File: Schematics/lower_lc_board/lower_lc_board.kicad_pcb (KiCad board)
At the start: 4 copper layers, 69.5 x 60 mm, 178 parts, among them J1 Stack Male Edge Connector, J10 SOL_CONN, J11 Screw_Terminal_01x02, J2 SWD_CONN, J3 USB_C_CONN, J4 HALL-1, J5 HALL-2, J6 PT1, J7 Screw_Terminal_01x02, J8 PT1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

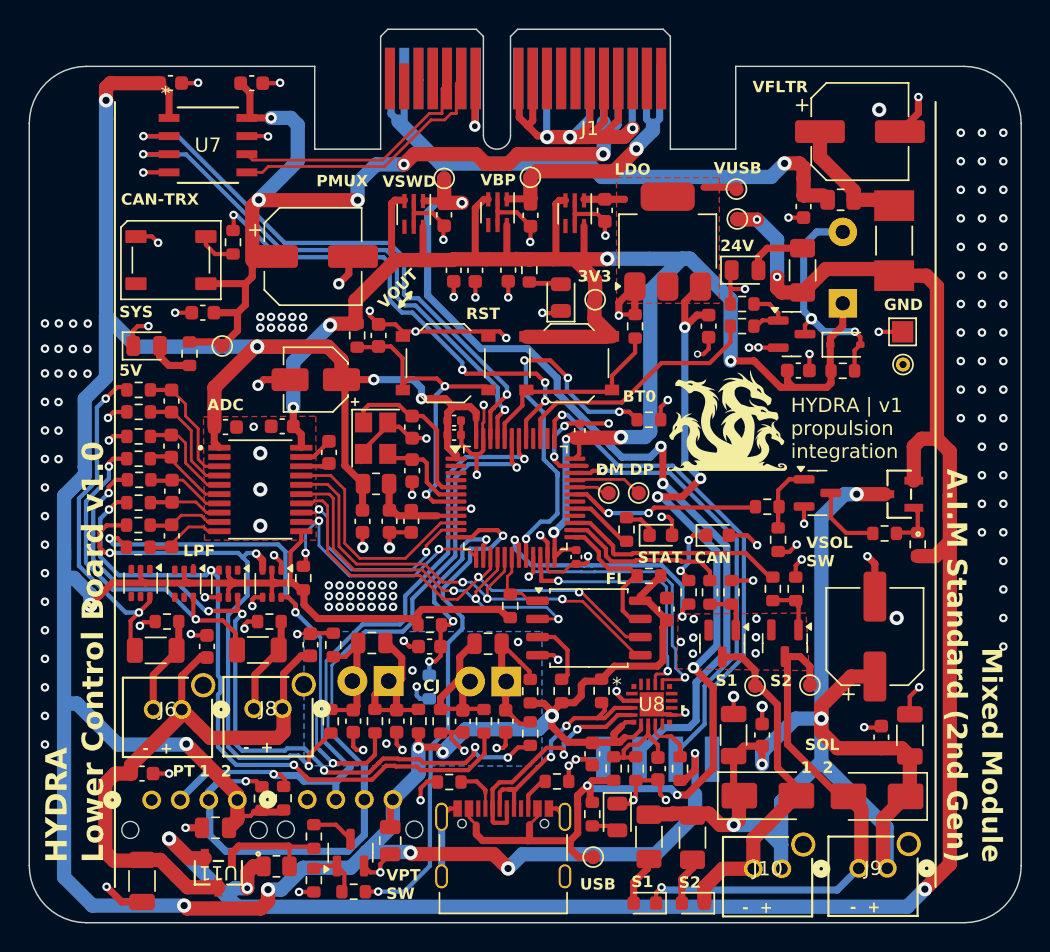
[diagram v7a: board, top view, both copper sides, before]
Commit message: increase width on power rails from USB and SWD, start tuning diff pairs
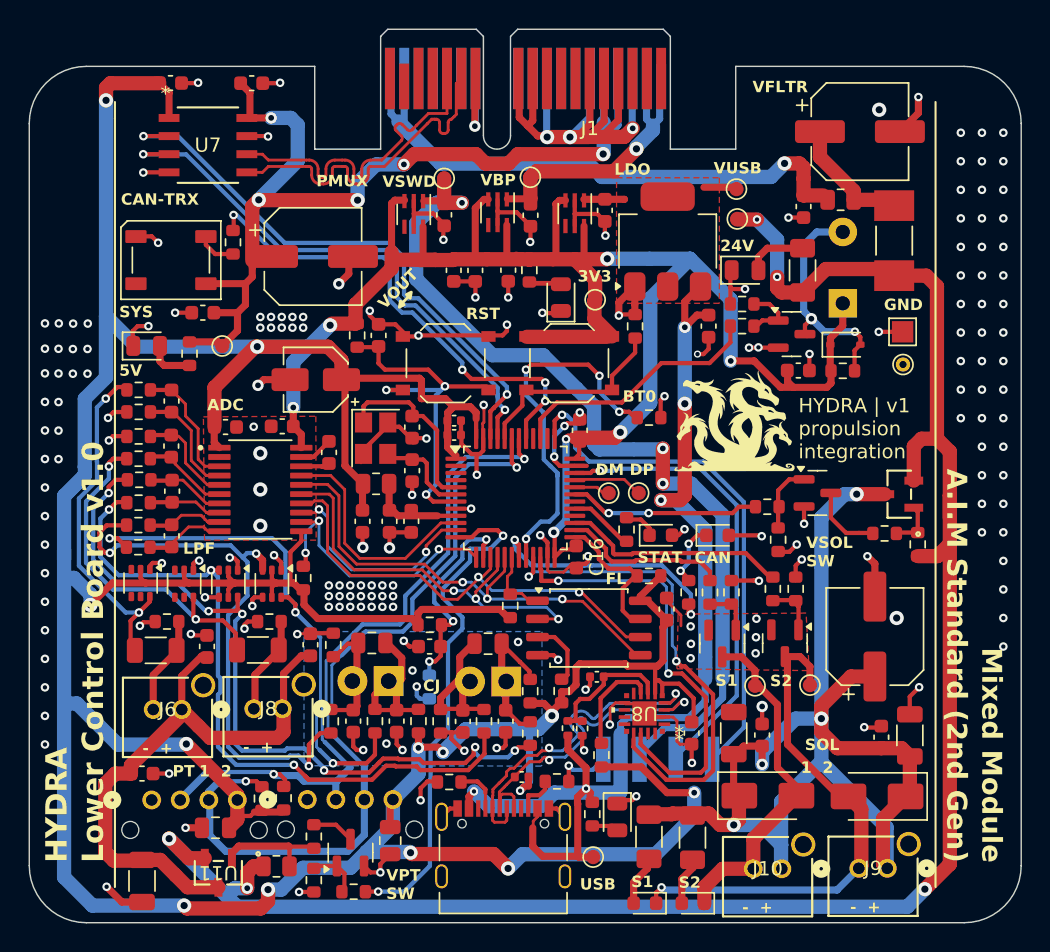
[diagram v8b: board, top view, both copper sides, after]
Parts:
- C15, C16: footprint Capacitor_SMD:C_0402_1005Metric -> Capacitor_SMD:C_0603_1608Metric
- C20: footprint Capacitor_SMD:C_0603_1608Metric -> Capacitor_SMD:C_0402_1005Metric
- R11, R12: footprint Resistor_SMD:R_0603_1608Metric -> Resistor_SMD:R_0402_1005Metric
- R21: value 10K -> 10k
- R23: value 4.7K -> 4.7k
- R45: footprint Resistor_SMD:R_0603_1608Metric -> Capacitor_SMD:C_0402_1005Metric
- moved R45 8.24 mm to (155.1, 97.3), turned to 0 degrees
- moved C20 7.72 mm to (160.4, 90.3), turned to 0 degrees
- moved C21 7.11 mm to (167.0, 94.3)
- moved R13 5.59 mm to (160.7, 95.8)
- moved R12 4.69 mm to (159.3, 93.9)
- moved R11 4.28 mm to (158.3, 93.9)
- moved U8 0.82 mm to (163.7, 92.9), turned to 180 degrees
- moved G*** 0.53 mm to (170.1, 72.4)
- moved R60 0.15 mm to (164.0, 72.2)
- moved C42 0.14 mm to (170.0, 94.3)
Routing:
- net USART_RX: track 18.3 -> 31.6 mm
- net USART_TX: track 20.8 -> 33.8 mm
- net USB_P: track 17.7 -> 24.9 mm
- net USB_N: track 17.8 -> 23.3 mm
- net CAN_P: track 17.8 -> 23.1 mm
- net CAN_N: track 19.0 -> 24.0 mm
- net STM_RESET: track 22.4 -> 26.7 mm, vias 2 -> 3
- net +3V3: track 431.5 -> 435.2 mm, vias 21 -> 20
- net Net-(U8-~{RST}): track 3.54 -> 7.14 mm
- net 5V_USB: track 73.5 -> 76.7 mm, vias 6 -> 5
- net V_SWD: track 62.0 -> 64.7 mm
- net Net-(U8-VBUS): track 6.80 -> 9.44 mm
- net SWCLK: track 34.6 -> 37.0 mm
- net +24V: track 135.4 -> 133.7 mm
- net SWDIO: track 30.6 -> 32.1 mm
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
